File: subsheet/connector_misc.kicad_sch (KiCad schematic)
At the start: 1 part, among them J1303 Conn_01x10

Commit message: Add order codes for all components
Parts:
- J1303: JLCPCB_IGNORE (none) -> 1
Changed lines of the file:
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@@
+			)
+		)
+		(property "I2C address" ""
+			(at 134.62 104.14 0)
+			(effects
+				(font
+					(size 1.27 1.27)
+				)
+				(hide yes)
+			)
+		)
+		(property "JLCPCB_IGNORE" "1"
+			(at 134.62 104.14 0)
+			(effects
+				(font
+					(size 1.27 1.27)
+				)
+				(hide yes)
 			)
 		)

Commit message: Silkscreen work. Edit tittle block/version number
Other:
- company: (c) -> (c) Vincent Dalstra
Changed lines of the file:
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@@
 	(title_block
 		(title "Untitled 4-layer JLCPCB")
-		(date "1984/04/01")
-		(rev "v1.0.0")
-		(company "(c)")
+		(date "2024-06-14")
+		(rev "1.0.0")
+		(company "(c) Vincent Dalstra")
 	)
 	(wire

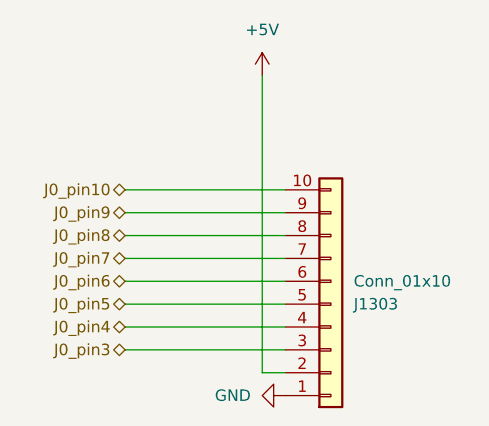
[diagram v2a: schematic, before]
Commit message: Move all subsheets into 'main' subsheet, below root
Keeping all the subsheets in a dedicated 'subsheet' folder makes things
much, much neater. However, specifying filepaths for subsheets has an
interesting problem; they use paths RELATIVE TO THE PARENT SHEET.

The consequence of is that if a subsheet is part of the root sheet, it
needs to be prefixed with 'subsheet/', but NOT if it's further down.
This inconsistency can be resolved by having a single 'main' sheet at
the top that doesn't move.

It's also useful to have a top-level space to put down changelogs,
descriptions etc.
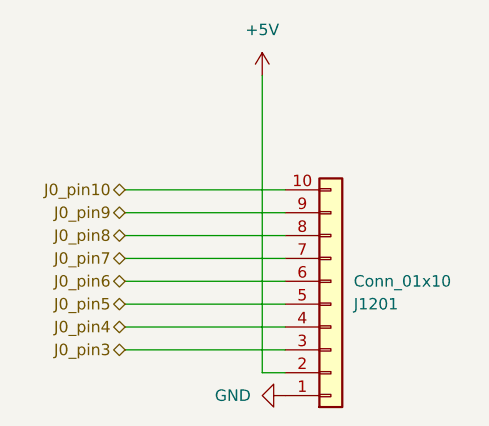
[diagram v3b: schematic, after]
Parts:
- renumbered J1303 to J1201
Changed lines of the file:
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@@
 		(shape bidirectional)
 		(at 111.76 93.98 180)
-		(fields_autoplaced yes)
 		(effects
 			(font
@@
 		(shape bidirectional)
 		(at 111.76 109.22 180)
-		(fields_autoplaced yes)
 		(effects
 			(font
@@
 		(shape bidirectional)
 		(at 111.76 96.52 180)
-		(fields_autoplaced yes)
 		(effects
 			(font
@@
 		(shape bidirectional)
 		(at 111.76 91.44 180)
-		(fields_autoplaced yes)
 		(effects
 			(font
@@
 		(shape bidirectional)
 		(at 111.76 101.6 180)
-		(fields_autoplaced yes)
 		(effects
 			(font
@@
 		(shape bidirectional)
 		(at 111.76 99.06 180)
-		(fields_autoplaced yes)
 		(effects
 			(font
@@
 		(shape bidirectional)
 		(at 111.76 104.14 180)
-		(fields_autoplaced yes)
 		(effects
 			(font
@@
 		(shape bidirectional)
 		(at 111.76 106.68 180)
-		(fields_autoplaced yes)
 		(effects
 			(font
@@
 		(dnp no)
 		(fields_autoplaced yes)
-		(property "Reference" "#PWR01307"
+		(property "Reference" "#PWR1201"
 			(at 127 82.55 0)
 			(effects
@@
 		(instances
 			(project "ESP_bare_chip_test_board"
-				(path "/45b6f84a-e69b-48be-a49b-bc68872e2c15/46d0c642-89b8-4065-a9ca-91ebde06cf7e"
-					(reference "#PWR01307")
+				(path "/45b6f84a-e69b-48be-a49b-bc68872e2c15/f48098a1-cacc-4192-b650-2a34a2ba76dc/23fb9360-5d8e-41d6-ba4b-d5d12818d2b1"
+					(reference "#PWR1201")
 					(unit 1)
 				)
@@
 		(on_board yes)
 		(dnp no)
-		(property "Reference" "J1303"
+		(property "Reference" "J1201"
 			(at 137.16 104.1401 0)
 			(effects
@@
 		(instances
 			(project "ESP_bare_chip_test_board"
-				(path "/45b6f84a-e69b-48be-a49b-bc68872e2c15/46d0c642-89b8-4065-a9ca-91ebde06cf7e"
-					(reference "J1303")
+				(path "/45b6f84a-e69b-48be-a49b-bc68872e2c15/f48098a1-cacc-4192-b650-2a34a2ba76dc/23fb9360-5d8e-41d6-ba4b-d5d12818d2b1"
+					(reference "J1201")
 					(unit 1)
 				)
@@
 		(on_board yes)
 		(dnp no)
-		(property "Reference" "#PWR01306"
+		(property "Reference" "#PWR1202"
 			(at 123.19 114.3 0)
 			(effects
@@
 		(instances
 			(project "ESP_bare_chip_test_board"
-				(path "/45b6f84a-e69b-48be-a49b-bc68872e2c15/46d0c642-89b8-4065-a9ca-91ebde06cf7e"
-					(reference "#PWR01306")
+				(path "/45b6f84a-e69b-48be-a49b-bc68872e2c15/f48098a1-cacc-4192-b650-2a34a2ba76dc/23fb9360-5d8e-41d6-ba4b-d5d12818d2b1"
+					(reference "#PWR1202")
 					(unit 1)
 				)
